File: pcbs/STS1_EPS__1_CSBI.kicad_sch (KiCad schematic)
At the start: 6 parts

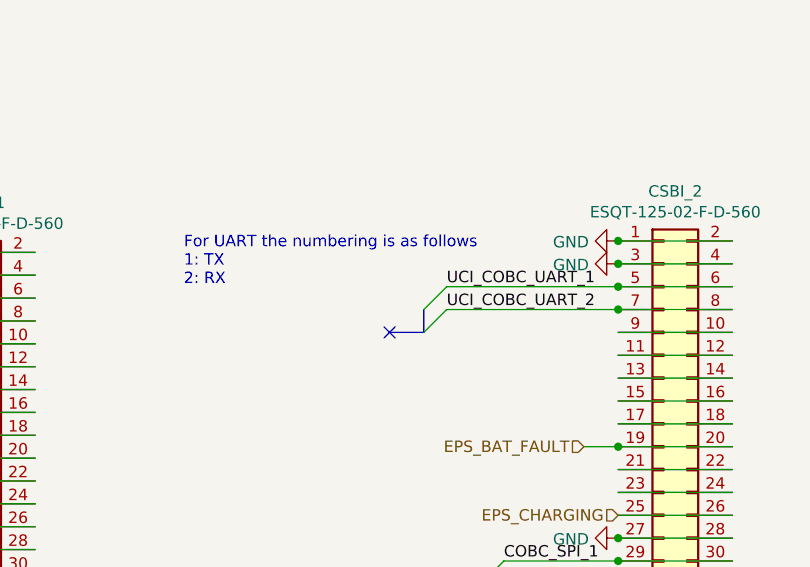
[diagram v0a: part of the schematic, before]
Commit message: Removed UCI connector from STS1_EPS_2 and merged UCI connector with J5 on STS1_EPS_1.
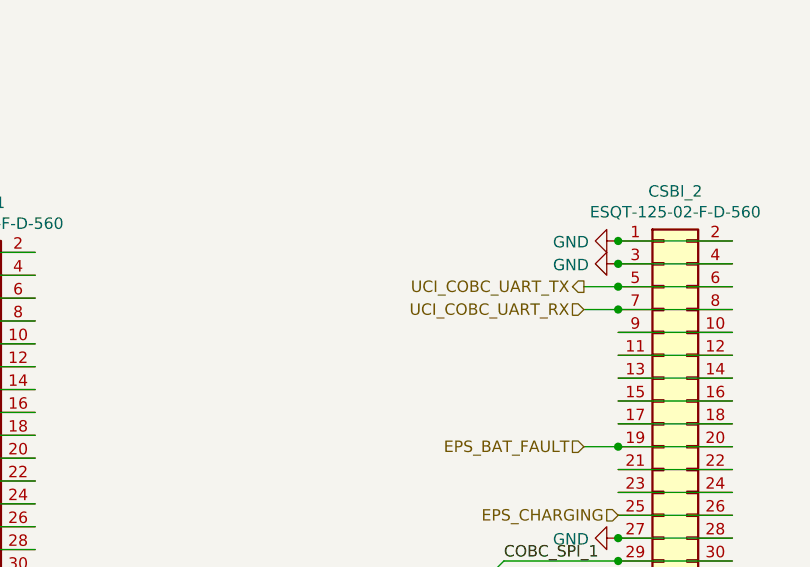
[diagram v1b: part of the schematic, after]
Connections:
- net UCI_COBC_UART_1 renamed UCI_COBC_UART_TX
- net UCI_COBC_UART_2 renamed UCI_COBC_UART_RX
- no-connect marks 2 -> 1
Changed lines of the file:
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@@
 		(at 62.23 102.87)
 	)
-	(no_connect
-		(at 139.7 53.34)
-	)
 	(bus_entry
 		(at 149.86 93.98)
@@
 	)
 	(bus_entry
-		(at 143.51 50.8)
-		(size 2.54 -2.54)
-		(stroke
-			(width 0)
-			(type default)
-		)
-	)
-	(bus_entry
 		(at 67.31 64.77)
 		(size 2.54 -2.54)
@@
 	)
 	(bus_entry
-		(at 143.51 53.34)
-		(size 2.54 -2.54)
-		(stroke
-			(width 0)
-			(type default)
-		)
-	)
-	(bus_entry
 		(at 67.31 67.31)
 		(size 2.54 -2.54)
@@
 		)
 	)
-	(bus
-		(pts
-			(xy 143.51 53.34) (xy 139.7 53.34)
-		)
-		(stroke
-			(width 0)
-			(type default)
-		)
-	)
 	(wire
 		(pts
@@
 		)
 	)
-	(bus
-		(pts
-			(xy 143.51 50.8) (xy 143.51 53.34)
-		)
-		(stroke
-			(width 0)
-			(type default)
-		)
-	)
 	(wire
 		(pts
@@
 	(wire
 		(pts
-			(xy 146.05 50.8) (xy 165.1 50.8)
+			(xy 161.29 50.8) (xy 165.1 50.8)
 		)
 		(stroke
@@
 	(wire
 		(pts
-			(xy 146.05 48.26) (xy 165.1 48.26)
+			(xy 161.29 48.26) (xy 165.1 48.26)
 		)
 		(stroke
@@
 	(text "For UART the numbering is as follows\n1: TX\n2: RX\n"
 		(exclude_from_sim no)
-		(at 116.84 48.26 0)
-		(effects
-			(font
-				(size 1.27 1.27)
-			)
-			(justify left bottom)
-		)
-	)
-	(text "For UART the numbering is as follows\n1: TX\n2: RX\n"
-		(exclude_from_sim no)
 		(at 35.56 110.49 0)
 		(effects
@@
 		)
 	)
-	(label "UCI_COBC_UART_2"
-		(at 146.05 50.8 0)
-		(fields_autoplaced yes)
-		(effects
-			(font
-				(size 1.27 1.27)
-			)
-			(justify left bottom)
-		)
-	)
 	(label "COBC_SPI_5"
 		(at 152.4 88.9 0)
@@
 	(label "COBC_SPI_2"
 		(at 152.4 81.28 0)
-		(fields_autoplaced yes)
-		(effects
-			(font
-				(size 1.27 1.27)
-			)
-			(justify left bottom)
-		)
-	)
-	(label "UCI_COBC_UART_1"
-		(at 146.05 48.26 0)
 		(fields_autoplaced yes)
 		(effects
@@
 		)
 	)
+	(hierarchical_label "UCI_COBC_UART_TX"
+		(shape output)
+		(at 161.29 48.26 180)
+		(fields_autoplaced yes)
+		(effects
+			(font
+				(size 1.27 1.27)
+			)
+			(justify right)
+		)
+	)
 	(hierarchical_label "EPS_CHARGING"
 		(shape input)
@@
 		(fields_autoplaced yes)
 		(effects
+			(font
+				(size 1.27 1.27)
+			)
+			(justify right)
+		)
+	)
+	(hierarchical_label "UCI_COBC_UART_RX"
+		(shape input)
+		(at 161.29 50.8 180)
+		(fields_autoplaced yes)
+		(effects

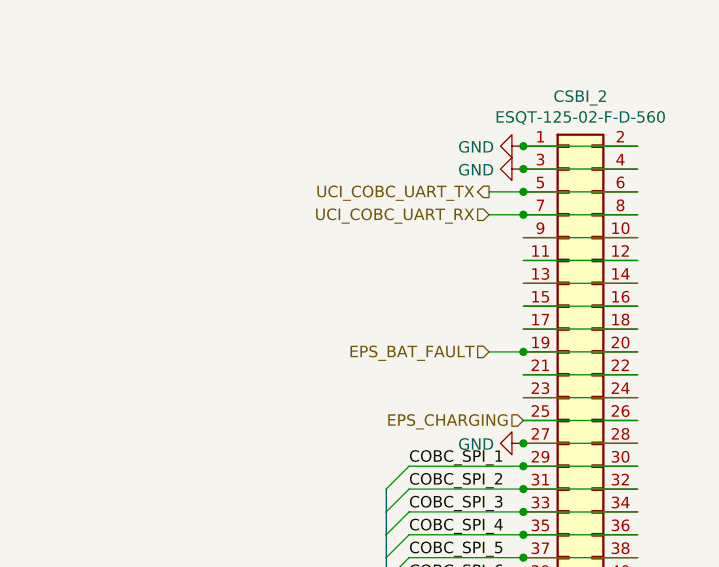
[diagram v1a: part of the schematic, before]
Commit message: Added even more ESD protection.
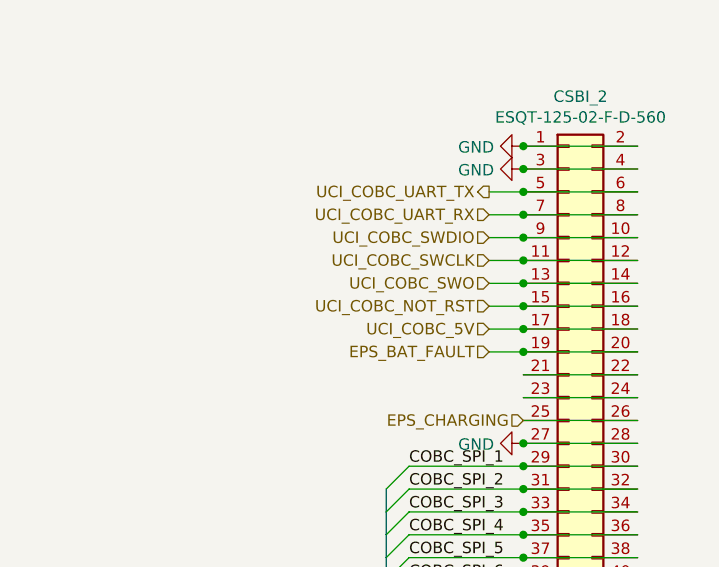
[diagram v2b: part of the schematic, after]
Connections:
- net UCI_COBC_SWDIO: now reaches CSBI_2.10 (Pin_10), CSBI_2.9 (Pin_9)
- net UCI_COBC_SWCLK: now reaches CSBI_2.11 (Pin_11), CSBI_2.12 (Pin_12)
- net UCI_COBC_SWO: now reaches CSBI_2.13 (Pin_13), CSBI_2.14 (Pin_14)
- net UCI_COBC_NOT_RST: now reaches CSBI_2.15 (Pin_15), CSBI_2.16 (Pin_16)
- net UCI_COBC_5V: now reaches CSBI_2.17 (Pin_17), CSBI_2.18 (Pin_18)

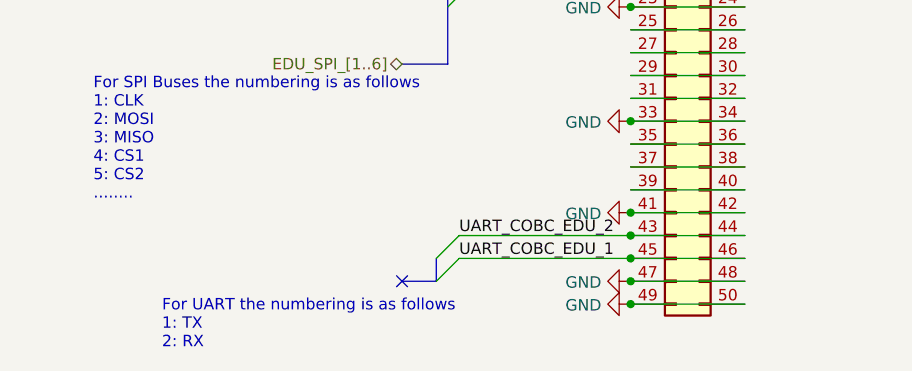
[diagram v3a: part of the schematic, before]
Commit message: Fixed warnings and errors.
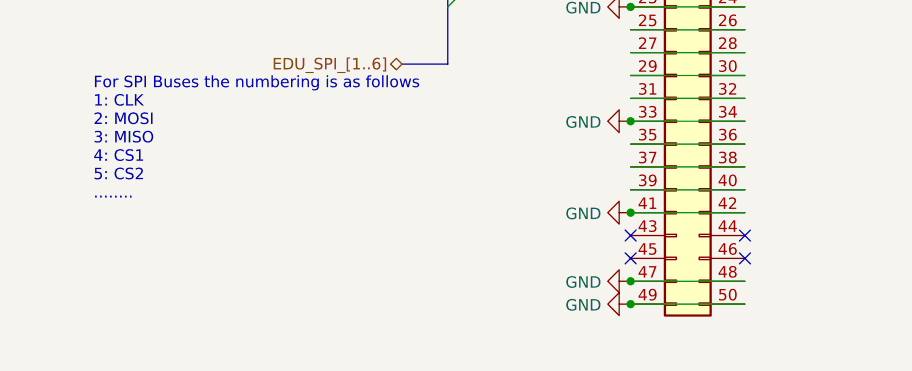
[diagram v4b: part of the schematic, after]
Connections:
- net UART_COBC_EDU_1: no longer names the net of CSBI_1.45 (Pin_45)
- net UART_COBC_EDU_1: no longer CSBI_1.46 (Pin_46)
- net UART_COBC_EDU_2: no longer names the net of CSBI_1.43 (Pin_43)
- net UART_COBC_EDU_2: no longer CSBI_1.44 (Pin_44)
- no-connect marks 1 -> 4
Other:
- note removed: "For UART the numbering is as follows 1: TX 2: RX"
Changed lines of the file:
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@@
 	)
 	(junction
+		(at 165.1 78.74)
+		(diameter 0)
+		(color 0 0 0 0)
+	)
+	(junction
+		(at 165.1 63.5)
+		(diameter 0)
+		(color 0 0 0 0)
+	)
+	(junction
+		(at 165.1 101.6)
+		(diameter 0)
+		(color 0 0 0 0)
+	)
+	(junction
+		(at 165.1 83.82)
+		(diameter 0)
+		(color 0 0 0 0)
+	)
+	(junction
+		(at 165.1 91.44)
+		(diameter 0)
+		(color 0 0 0 0)
+	)
+	(junction
+		(at 87.63 67.31)
+		(diameter 0)
+		(color 0 0 0 0)
+	)
+	(junction
+		(at 165.1 48.26)
+		(diameter 0)
+		(color 0 0 0 0)
+	)
+	(junction
+		(at 87.63 102.87)
+		(diameter 0)
+		(color 0 0 0 0)
+	)
+	(junction
+		(at 165.1 53.34)
+		(diameter 0)
+		(color 0 0 0 0)
+	)
+	(junction
+		(at 87.63 57.15)
+		(diameter 0)
+		(color 0 0 0 0)
+	)
+	(junction
+		(at 87.63 72.39)
+		(diameter 0)
+		(color 0 0 0 0)
+	)
+	(junction
+		(at 87.63 44.45)
+		(diameter 0)
+		(color 0 0 0 0)
+	)
+	(junction
+		(at 87.63 95.25)
+		(diameter 0)
+		(color 0 0 0 0)
+	)
+	(junction
+		(at 165.1 66.04)
+		(diameter 0)
+		(color 0 0 0 0)
+	)
+	(junction
+		(at 165.1 55.88)
+		(diameter 0)
+		(color 0 0 0 0)
+	)
+	(junction
+		(at 165.1 50.8)
+		(diameter 0)
+		(color 0 0 0 0)
+	)
+	(junction
+		(at 87.63 62.23)
+		(diameter 0)
+		(color 0 0 0 0)
+	)
+	(junction
+		(at 165.1 76.2)
+		(diameter 0)
+		(color 0 0 0 0)
+	)
+	(junction
+		(at 87.63 105.41)
+		(diameter 0)
+		(color 0 0 0 0)
+	)
+	(junction
+		(at 87.63 85.09)
+		(diameter 0)
+		(color 0 0 0 0)
+	)
+	(junction
+		(at 165.1 60.96)
+		(diameter 0)
+		(color 0 0 0 0)
+	)
+	(junction
+		(at 165.1 88.9)
+		(diameter 0)
+		(color 0 0 0 0)
+	)
+	(junction
+		(at 87.63 46.99)
+		(diameter 0)
+		(color 0 0 0 0)
+	)
+	(junction
+		(at 165.1 81.28)
+		(diameter 0)
+		(color 0 0 0 0)
+	)
+	(junction
+		(at 87.63 64.77)
+		(diameter 0)
+		(color 0 0 0 0)
+	)
+	(junction
+		(at 87.63 59.69)
+		(diameter 0)
+		(color 0 0 0 0)
+	)
+	(junction
+		(at 87.63 54.61)
+		(diameter 0)
+		(color 0 0 0 0)
+	)
+	(junction
+		(at 165.1 43.18)
+		(diameter 0)
+		(color 0 0 0 0)
+	)
+	(junction
+		(at 165.1 104.14)
+		(diameter 0)
+		(color 0 0 0 0)
+	)
+	(junction
+		(at 165.1 86.36)
+		(diameter 0)
+		(color 0 0 0 0)
+	)
+	(no_connect
+		(at 100.33 100.33)
+	)
+	(no_connect
+		(at 87.63 97.79)
+	)
+	(no_connect
+		(at 100.33 97.79)
+	)
+	(no_connect
 		(at 87.63 100.33)
-		(diameter 0)
-		(color 0 0 0 0)
-	)
-	(junction
-		(at 165.1 78.74)
-		(diameter 0)
-		(color 0 0 0 0)
-	)
-	(junction
-		(at 165.1 63.5)
-		(diameter 0)
-		(color 0 0 0 0)
-	)
-	(junction
-		(at 165.1 101.6)
-		(diameter 0)
-		(color 0 0 0 0)
-	)
-	(junction
-		(at 165.1 83.82)
-		(diameter 0)
-		(color 0 0 0 0)
-	)
-	(junction
-		(at 165.1 91.44)
-		(diameter 0)
-		(color 0 0 0 0)
-	)
-	(junction
-		(at 87.63 67.31)
-		(diameter 0)
-		(color 0 0 0 0)
-	)
-	(junction
-		(at 165.1 48.26)
-		(diameter 0)
-		(color 0 0 0 0)
-	)
-	(junction
-		(at 87.63 102.87)
-		(diameter 0)
-		(color 0 0 0 0)
-	)
-	(junction
-		(at 165.1 53.34)
-		(diameter 0)
-		(color 0 0 0 0)
-	)
-	(junction
-		(at 87.63 97.79)
-		(diameter 0)
-		(color 0 0 0 0)
-	)
-	(junction
-		(at 87.63 57.15)
-		(diameter 0)
-		(color 0 0 0 0)
-	)
-	(junction
-		(at 87.63 72.39)
-		(diameter 0)
-		(color 0 0 0 0)
-	)
-	(junction
-		(at 87.63 44.45)
-		(diameter 0)
-		(color 0 0 0 0)
-	)
-	(junction
-		(at 87.63 95.25)
-		(diameter 0)
-		(color 0 0 0 0)
-	)
-	(junction
-		(at 165.1 66.04)
-		(diameter 0)
-		(color 0 0 0 0)
-	)
-	(junction
-		(at 165.1 55.88)
-		(diameter 0)
-		(color 0 0 0 0)
-	)
-	(junction
-		(at 165.1 50.8)
-		(diameter 0)
-		(color 0 0 0 0)
-	)
-	(junction
-		(at 87.63 62.23)
-		(diameter 0)
-		(color 0 0 0 0)
-	)
-	(junction
-		(at 165.1 76.2)
-		(diameter 0)
-		(color 0 0 0 0)
-	)
-	(junction
-		(at 87.63 105.41)
-		(diameter 0)
-		(color 0 0 0 0)
-	)
-	(junction
-		(at 87.63 85.09)
-		(diameter 0)
-		(color 0 0 0 0)
-	)
-	(junction
-		(at 165.1 60.96)
-		(diameter 0)
-		(color 0 0 0 0)
-	)
-	(junction
-		(at 165.1 88.9)
-		(diameter 0)
-		(color 0 0 0 0)
-	)
-	(junction
-		(at 87.63 46.99)
-		(diameter 0)
-		(color 0 0 0 0)
-	)
-	(junction
-		(at 165.1 81.28)
-		(diameter 0)
-		(color 0 0 0 0)
-	)
-	(junction
-		(at 87.63 64.77)
-		(diameter 0)
-		(color 0 0 0 0)
-	)
-	(junction
-		(at 87.63 59.69)
-		(diameter 0)
-		(color 0 0 0 0)
-	)
-	(junction
-		(at 87.63 54.61)
-		(diameter 0)
-		(color 0 0 0 0)
-	)
-	(junction
-		(at 165.1 43.18)
-		(diameter 0)
-		(color 0 0 0 0)
-	)
-	(junction
-		(at 165.1 104.14)
-		(diameter 0)
-		(color 0 0 0 0)
-	)
-	(junction
-		(at 165.1 86.36)
-		(diameter 0)
-		(color 0 0 0 0)
-	)
-	(no_connect
-		(at 62.23 102.87)
 	)
 	(bus_entry
@@
 	)
 	(bus_entry
-		(at 66.04 102.87)
-		(size 2.54 -2.54)
-		(stroke
-			(width 0)
-			(type default)
-		)
-	)
-	(bus_entry
 		(at 149.86 81.28)
 		(size 2.54 -2.54)
@@
 	)
 	(bus_entry
-		(at 66.04 100.33)
-		(size 2.54 -2.54)
-		(stroke
-			(width 0)
-			(type default)
-		)
-	)
-	(bus_entry
 		(at 67.31 67.31)
 		(size 2.54 -2.54)
@@
 	(wire
 		(pts
-			(xy 68.58 100.33) (xy 87.63 100.33)
-		)
-		(stroke
-			(width 0)
-			(type default)
-		)
-	)
-	(wire
-		(pts
 			(xy 87.63 64.77) (xy 100.33 64.77)
 		)
@@
 	(wire
 		(pts
-			(xy 87.63 97.79) (xy 100.33 97.79)
-		)
-		(stroke
-			(width 0)
-			(type default)
-		)
-	)
-	(wire
-		(pts
 			(xy 87.63 59.69) (xy 100.33 59.69)
 		)
@@
 	(wire
 		(pts
-			(xy 87.63 100.33) (xy 100.33 100.33)
-		)
-		(stroke
-			(width 0)
-			(type default)
-		)
-	)
-	(wire
-		(pts
 			(xy 161.29 66.04) (xy 165.1 66.04)
 		)
@@
 	(wire
 		(pts
-			(xy 68.58 97.79) (xy 87.63 97.79)
-		)
-		(stroke
-			(width 0)
-			(type default)
-		)
-	)
-	(wire
-		(pts
 			(xy 165.1 99.06) (xy 177.8 99.06)
 		)
@@
 	(bus
 		(pts
-			(xy 66.04 100.33) (xy 66.04 102.87)
-		)
-		(stroke
-			(width 0)
-			(type default)
-		)
-	)
-	(bus
-		(pts
 			(xy 149.86 88.9) (xy 149.86 91.44)
 		)
@@
 		(pts
 			(xy 87.63 57.15) (xy 100.33 57.15)
-		)
-		(stroke
-			(width 0)
-			(type default)
-		)
-	)
-	(bus
-		(pts
-			(xy 66.04 102.87) (xy 62.23 102.87)
 		)
 		(stroke
@@
 		)
 	)
-	(text "For UART the numbering is as follows\n1: TX\n2: RX\n"
-		(exclude_from_sim no)
-		(at 35.56 110.49 0)
-		(effects
-			(font
-				(size 1.27 1.27)
-			)
-			(justify left bottom)
-		)
-	)
 	(label "EDU_SPI_2"
 		(at 73.66 67.31 0)
@@
 		)
 	)
-	(label "UART_COBC_EDU_1"
-		(at 68.58 100.33 0)
-		(fields_autoplaced yes)
-		(effects
-			(font
-				(size 1.27 1.27)
-			)
-			(justify left bottom)
-		)
-	)
 	(label "COBC_SPI_3"
 		(at 152.4 83.82 0)
@@
 		(fields_autoplaced yes)
 		(effects
-			(font
-				(size 1.27 1.27)
-			)
-			(justify left bottom)
-		)
-	)
-	(label "UART_COBC_EDU_2"
-		(at 68.58 97.79 0)
-		(fields_autoplaced yes)
-		(effects

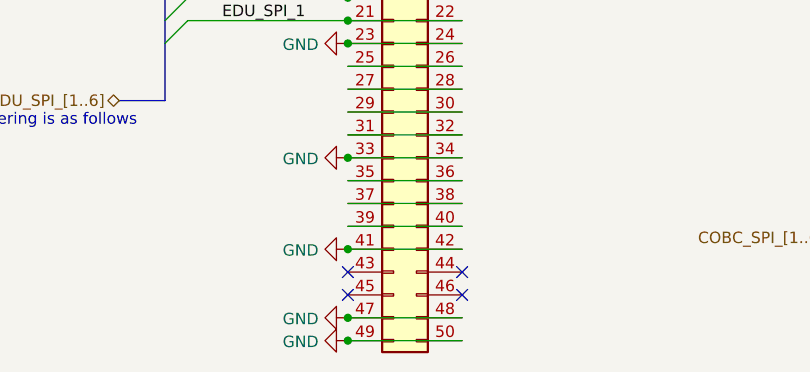
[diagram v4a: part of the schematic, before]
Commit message: STS1_EPS_1 now without errors.
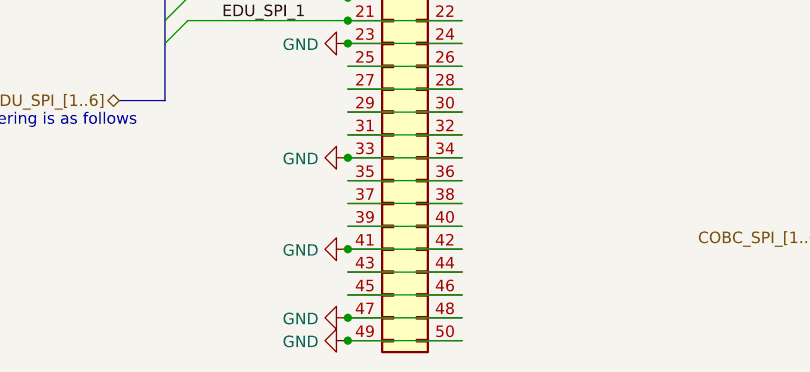
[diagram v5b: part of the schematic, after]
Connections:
- net at CSBI_1.43 (Pin_43): now also CSBI_1.44 (Pin_44)
- net at CSBI_1.45 (Pin_45): now also CSBI_1.46 (Pin_46)
- no-connect marks 4 -> 0
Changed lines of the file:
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@@
 		(color 0 0 0 0)
 	)
-	(no_connect
-		(at 100.33 100.33)
-	)
-	(no_connect
-		(at 87.63 97.79)
-	)
-	(no_connect
-		(at 100.33 97.79)
-	)
-	(no_connect
-		(at 87.63 100.33)
-	)
 	(bus_entry
 		(at 149.86 93.98)
@@
 	(wire
 		(pts
+			(xy 87.63 97.79) (xy 100.33 97.79)
+		)
+		(stroke
+			(width 0)
+			(type default)
+		)
+	)
+	(wire
+		(pts
 			(xy 87.63 52.07) (xy 100.33 52.07)
 		)
@@
 		)
 		(stroke
+			(width 0)
+			(type default)
+		)
+	)
+	(wire
+		(pts
+			(xy 87.63 100.33) (xy 100.33 100.33)
+		)
+		(stroke

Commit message: Added part numbers to components of STS1_EPS_1.
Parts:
- CSBI_1, CSBI_2: Part Nr. (none) -> ESQT-125-02-F-D-560
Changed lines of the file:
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@@
+			)
+		)
+		(property "Part Nr." "ESQT-125-02-F-D-560"
+			(at 92.71 74.93 0)
+			(effects
+				(font
+					(size 1.27 1.27)
+				)
+				(hide yes)
 			)
 		)
@@
 			(at 170.18 73.66 0)
 			(effects
+				(font
+					(size 1.27 1.27)
+				)
+				(hide yes)
+			)
+		)
+		(property "Part Nr." "ESQT-125-02-F-D-560"
+			(at 170.18 73.66 0)
+			(effects
